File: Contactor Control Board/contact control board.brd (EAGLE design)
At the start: 75.9 x 50.8 mm, 34 parts, among them Q1 2n2222, Q3 2n2222, Q4 MOSFET-NCHANNELFQP30N06L, Q5 MOSFET-NCHANNELFQP30N06L, U1 MM74HC125N

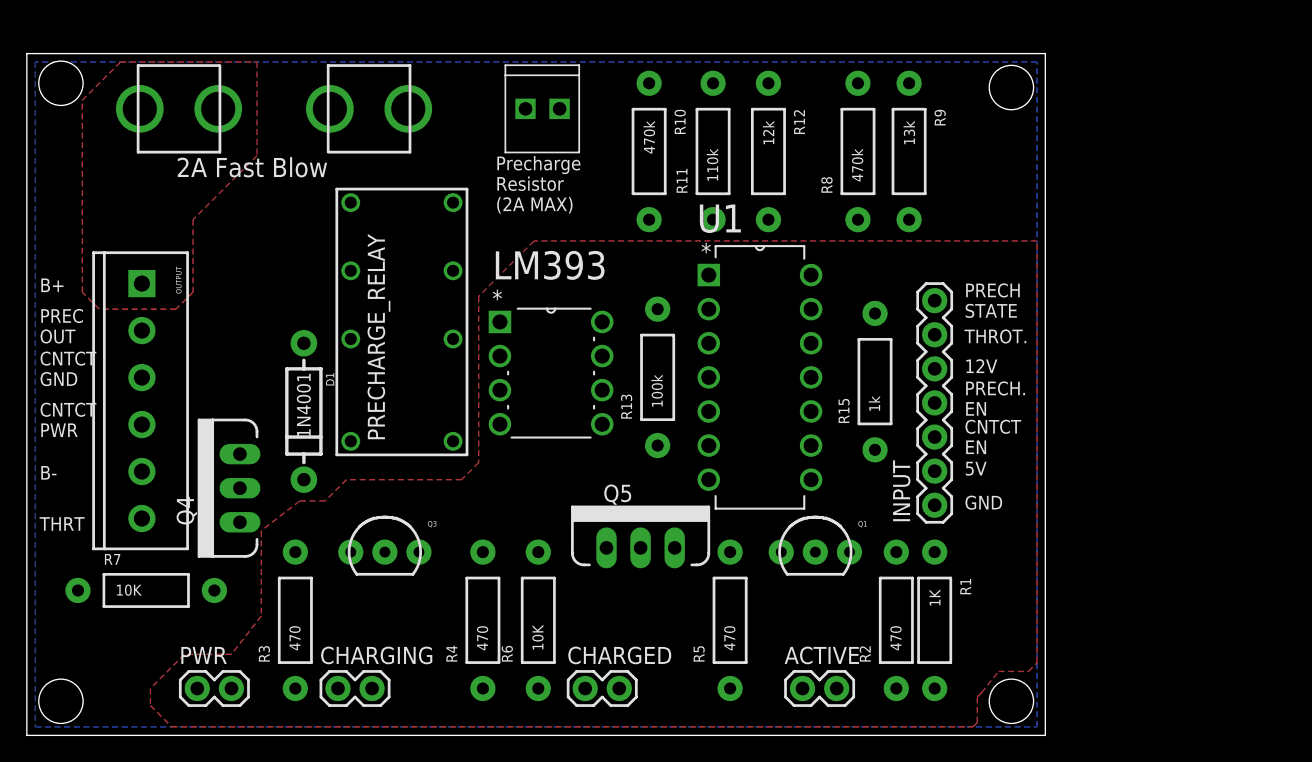
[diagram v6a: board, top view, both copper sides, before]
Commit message: Mostly routed. Replaced all thru-hole with SMD components. Much smaller!
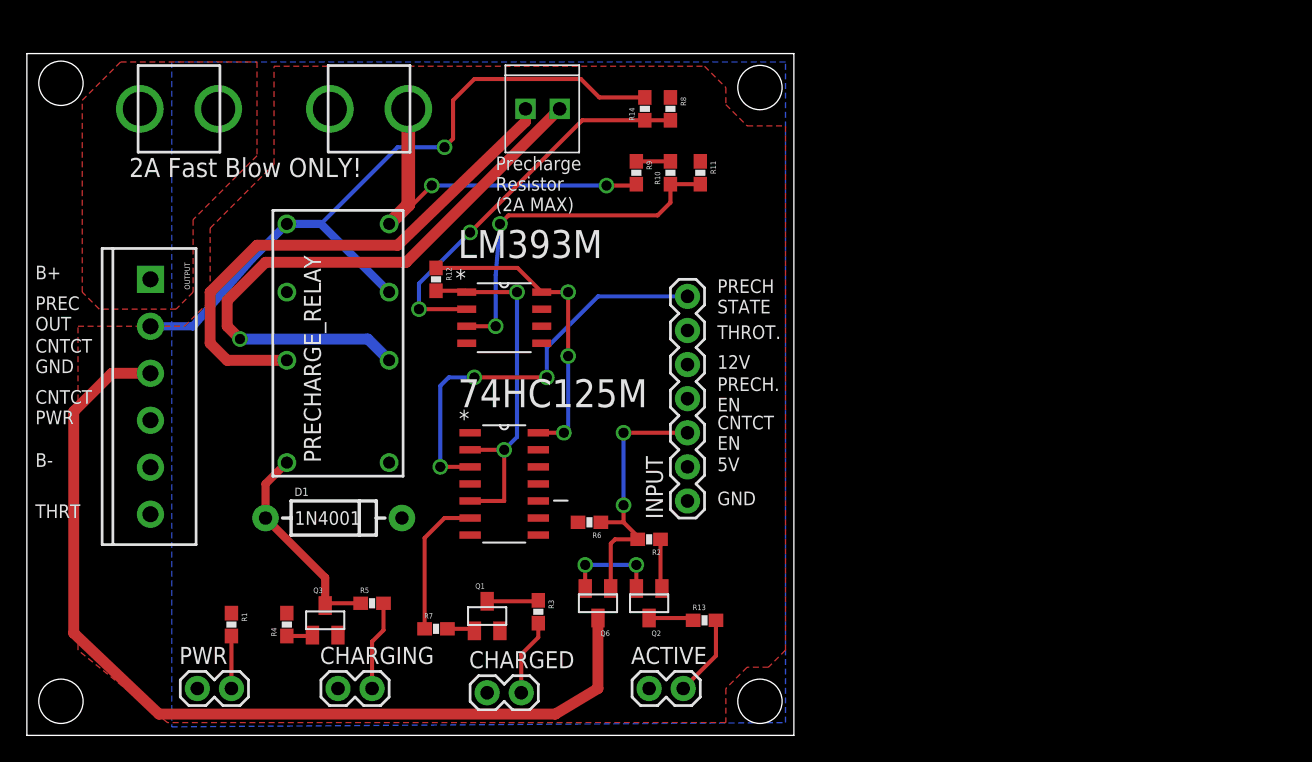
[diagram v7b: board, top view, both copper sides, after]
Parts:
- removed LM393: LM393AN, Fairchild_By_element14_Batch_1:DIP254P762X508-8
- removed Q4, Q5: MOSFET-NCHANNELFQP30N06L, SparkFun-DiscreteSemi:TO220V
- removed R15: 1k, SparkFun-Resistors:AXIAL-0.4
- removed U1: MM74HC125N, mm74hc125n:DIP254P762X533-14
- added 74HC125M: MM74HC125M, Fairchild_By_element14_Batch_1:SOIC127P600X175-14N
- added LM393M: LM393M, Fairchild_By_element14_Batch_1:SOIC127P600X180-8N
- added Q2: MMBT2222A, SparkFun-DiscreteSemi:SOT23
- added Q6: MOSFET-NCHANNELBSS123LT1G, SparkFun-DiscreteSemi:SOT23
- added R14: 470k, SparkFun-Resistors:0603-RES
- Q1: value 2n2222 -> MMBT2222A; device SparkFun-DiscreteSemi:TO-92-AMMO -> SparkFun-DiscreteSemi:SOT23
- Q3: value 2n2222 -> MOSFET-NCHANNELBSS123LT1G; device SparkFun-DiscreteSemi:TO-92-AMMO -> SparkFun-DiscreteSemi:SOT23
- R1: value 1K -> 470k; device SparkFun-Resistors:AXIAL-0.4 -> SparkFun-Resistors:0603-RES
- R10: value 470k -> 110k; device SparkFun-Resistors:AXIAL-0.4 -> SparkFun-Resistors:0603-RES
- R11: value 110k -> 12k; device SparkFun-Resistors:AXIAL-0.4 -> SparkFun-Resistors:0603-RES
- R12: value 12k -> 100k; device SparkFun-Resistors:AXIAL-0.4 -> SparkFun-Resistors:0603-RES
- R13: value 100k -> 470k; device SparkFun-Resistors:AXIAL-0.4 -> SparkFun-Resistors:0603-RES
- R2: value 470 -> 1k; device SparkFun-Resistors:AXIAL-0.4 -> SparkFun-Resistors:0603-RES
- R3, R5: value 470 -> 470k; device SparkFun-Resistors:AXIAL-0.4 -> SparkFun-Resistors:0603-RES
- R4: value 470 -> 10k; device SparkFun-Resistors:AXIAL-0.4 -> SparkFun-Resistors:0603-RES
- R6: value 10K -> 10k; device SparkFun-Resistors:AXIAL-0.4 -> SparkFun-Resistors:0603-RES
- R7: value 10K -> 1k; device SparkFun-Resistors:AXIAL-0.4 -> SparkFun-Resistors:0603-RES
- R8: value 470k -> 13k; device SparkFun-Resistors:AXIAL-0.4 -> SparkFun-Resistors:0603-RES
- R9: value 13k -> 470k; device SparkFun-Resistors:AXIAL-0.4 -> SparkFun-Resistors:0603-RES
- moved R1 52.4 mm to (15.2, 8.26)
- moved R5 26.7 mm to (25.7, 9.84), turned to 0 degrees
- moved R12 26.5 mm to (30.5, 34.0)
- moved Q1 24.9 mm to (34.3, 8.89)
- moved R7 21.8 mm to (30.5, 7.94)
- moved R9 20.4 mm to (45.4, 41.9)
- moved R2 19.4 mm to (46.4, 14.6), turned to 180 degrees
- moved STANDOFF3 18.7 mm to (54.6, 48.3)
- moved STANDOFF4 18.7 mm to (54.6, 2.54)
- moved R13 18.4 mm to (50.5, 8.57), turned to 0 degrees
- moved INPUT 18.4 mm to (49.2, 17.5)
- moved R3 18.1 mm to (38.1, 9.21), turned to 270 degrees
- moved R4 14.6 mm to (19.4, 8.26)
- moved R8 14.3 mm to (47.9, 46.7), turned to 270 degrees
- moved ACTIVE 11.4 mm to (46.4, 3.49)
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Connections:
- net 5V: now also 74HC125M.14, LM393M.8, R12.1; no longer LM393.8, R13.P$1, U1.14
- net 72V_IN_FUSED: now also R9.2; no longer R10.P$1
- net CAP_CHARGE_REF: now also LM393M.3, R10.1, R11.2; no longer LM393.3, R11.P$2, R12.P$1
- net CAP_CHARGE_V_CURR: now also LM393M.2, R14.1, R8.2; no longer LM393.2, R8.P$2, R9.P$1
- net CONTACT_EN: now also Q6.1, R2.2, R6.1; no longer Q4.1, R1.P$1, R7.P$2
- net CONTACT_GND: now also Q6.3; no longer Q4.2
- net GND: now also 74HC125M.1, 74HC125M.4, 74HC125M.7, LM393M.4, Q1.2, Q2.2, Q3.2, Q6.2, R1.1, R11.1, R4.2, R6.2, R8.1; no longer LM393.4, Q1.1, Q3.1, Q4.3, Q5.3, R12.P$2, R3.P$2, R6.P$1, R7.P$1, R9.P$2, U1.1, U1.4, U1.7
- net N$1: now also Q2.3, R13.1; no longer Q1.3, R2.P$2
- net N$12: now also R1.2; no longer R3.P$1
- net N$2: now also Q2.1, R2.1; no longer Q1.2, R1.P$2
- net N$3: now also R10.2, R9.1; no longer R10.P$2, R11.P$1
- net N$4: now also R3.2; no longer R5.P$1
- net N$5: now also Q1.3, R3.1; no longer Q3.3, R5.P$2
- net N$6: now also 74HC125M.6, R7.1; no longer R15.P$2, U1.6
- net N$7: now also R5.2; no longer R4.P$1
- net N$9: now also R13.2; no longer R2.P$1
- net PRECHARGE_EN: now also Q3.1, R4.1; no longer Q5.1, R6.P$2
- net PRECHARGE_OUT: now also R14.2; no longer R8.P$1
- net PRECH_DRAIN: now also Q3.3, R5.1; no longer Q5.2, R4.P$2
- net PRECH_STATE_LED: now also Q1.1, R7.2; no longer Q3.2, R15.P$1
- net PRECH_STATE_OUT: now also 74HC125M.3; no longer U1.3
- net PRECH_STATE_TO_BUFF: now also 74HC125M.2, 74HC125M.5, LM393M.1, R12.2; no longer LM393.1, R13.P$2, U1.2, U1.5
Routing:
- net CONTACT_GND: track 0.00 -> 70.6 mm
- net PRECHARGE_OUT: track 0.00 -> 54.1 mm, vias 0 -> 1
- net PRECHARGE_RESISTOR_IN: track 0.00 -> 45.7 mm, vias 0 -> 1
- net PRECHARGE_RESISTOR_OUT: track 0.00 -> 39.7 mm
- net PRECH_STATE_OUT: track 0.00 -> 30.7 mm, vias 0 -> 3
- net CAP_CHARGE_V_CURR: track 0.00 -> 29.2 mm, vias 0 -> 2
- net PRECH_STATE_TO_BUFF: track 0.00 -> 27.1 mm, vias 0 -> 2
- net 72V_IN_FUSED: track 0.00 -> 26.8 mm, vias 0 -> 2
- net CAP_CHARGE_REF: track 0.00 -> 26.7 mm, vias 0 -> 2
- net 5V: track 0.00 -> 23.1 mm, vias 0 -> 3
- net CONTACT_EN: track 0.00 -> 20.3 mm, vias 0 -> 2
- net PRECH_DRAIN: track 0.00 -> 15.9 mm
- net N$6: track 0.00 -> 10.8 mm
- net GND: track 0.00 -> 7.33 mm, vias 0 -> 2
- net N$7: track 0.00 -> 6.70 mm
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- added copper zone on layer 16, net 5V
- added copper zone on layer 1, net GND
- removed copper zone on layer 1, net 5V
- removed copper zone on layer 16, net GND
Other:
- board size 75.9 x 50.8 mm -> 57.1 x 50.8 mm
- board text added: "2A Fast Blow ONLY!"
- board text removed: "2A Fast Blow"

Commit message: Fixed values for FETs and some resistors whcih were cut and paste errors.
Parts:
- Q3, Q6: value MOSFET-NCHANNELBSS123LT1G -> IRLML6344TRPBF
- R1, R13, R3, R5: value 470k -> 470
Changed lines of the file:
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@@
 <layer number="23" name="tOrigins" color="15" fill="1" visible="yes" active="yes"/>
 <layer number="24" name="bOrigins" color="15" fill="1" visible="yes" active="yes"/>
-<layer number="25" name="tNames" color="16" fill="1" visible="yes" active="yes"/>
+<layer number="25" name="tNames" color="16" fill="1" visible="no" active="yes"/>
 <layer number="26" name="bNames" color="16" fill="1" visible="no" active="yes"/>
 <layer number="27" name="tValues" color="7" fill="1" visible="no" active="yes"/>
@@
 <element name="R11" library="SparkFun-Resistors" package="0603-RES" value="12k" x="50.165" y="41.91" rot="R270"/>
 <element name="R12" library="SparkFun-Resistors" package="0603-RES" value="100k" x="30.48" y="33.9725" rot="R270"/>
-<element name="R13" library="SparkFun-Resistors" package="0603-RES" value="470k" x="50.4825" y="8.5725"/>
+<element name="R13" library="SparkFun-Resistors" package="0603-RES" value="470" x="50.4825" y="8.5725"/>
 <element name="R2" library="SparkFun-Resistors" package="0603-RES" value="1k" x="46.355" y="14.605" rot="R180"/>
-<element name="R1" library="SparkFun-Resistors" package="0603-RES" value="470k" x="15.24" y="8.255" rot="R270"/>
-<element name="R3" library="SparkFun-Resistors" package="0603-RES" value="470k" x="38.1" y="9.2075" rot="R270"/>
-<element name="R5" library="SparkFun-Resistors" package="0603-RES" value="470k" x="25.7175" y="9.8425"/>
+<element name="R1" library="SparkFun-Resistors" package="0603-RES" value="470" x="15.24" y="8.255" rot="R270"/>
+<element name="R3" library="SparkFun-Resistors" package="0603-RES" value="470" x="38.1" y="9.2075" rot="R270"/>
+<element name="R5" library="SparkFun-Resistors" package="0603-RES" value="470" x="25.7175" y="9.8425"/>
 <element name="R4" library="SparkFun-Resistors" package="0603-RES" value="10k" x="19.3675" y="8.255" rot="R90"/>
 <element name="R6" library="SparkFun-Resistors" package="0603-RES" value="10k" x="41.91" y="15.875" rot="R180"/>
@@
 <attribute name="PROD_ID" value="TRANS-08049" x="34.29" y="8.89" size="1.778" layer="27" font="vector" ratio="15" display="off"/>
 </element>
-<element name="Q3" library="SparkFun-DiscreteSemi" package="SOT23" value="MOSFET-NCHANNELBSS123LT1G" x="22.225" y="8.5725">
+<element name="Q3" library="SparkFun-DiscreteSemi" package="SOT23" value="IRLML6344TRPBF" x="22.225" y="8.5725">
 <attribute name="PROD_ID" value="TRANS-08345" x="22.225" y="8.5725" size="1.778" layer="27" font="vector" ratio="15" display="off"/>
 </element>
-<element name="Q6" library="SparkFun-DiscreteSemi" package="SOT23" value="MOSFET-NCHANNELBSS123LT1G" x="42.545" y="9.8425" rot="R180">
+<element name="Q6" library="SparkFun-DiscreteSemi" package="SOT23" value="IRLML6344TRPBF" x="42.545" y="9.8425" rot="R180">
 <attribute name="PROD_ID" value="TRANS-08345" x="42.545" y="9.8425" size="1.778" layer="27" font="vector" ratio="15" rot="R180" display="off"/>
 </element>
